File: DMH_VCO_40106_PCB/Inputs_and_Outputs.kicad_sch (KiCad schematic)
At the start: 13 parts, among them J1 TS_Jack_6.35mm_Sw, J150 Conn_01x12, J2 TS_Jack_6.35mm_Sw, J200 IDC_02x05, J3 TS_Jack_6.35mm_Sw, J4 TS_Jack_6.35mm_Sw, J5 TS_Jack_6.35mm_Sw, J6 TS_Jack_6.35mm_Sw, J7 TS_Jack_6.35mm_Sw, J8 TS_Jack_6.35mm_Sw, J9 TS_Jack_6.35mm_Sw, SW1 SW_SPDT_321_OnOff, SW2 SW_SPDT_321_OnOff

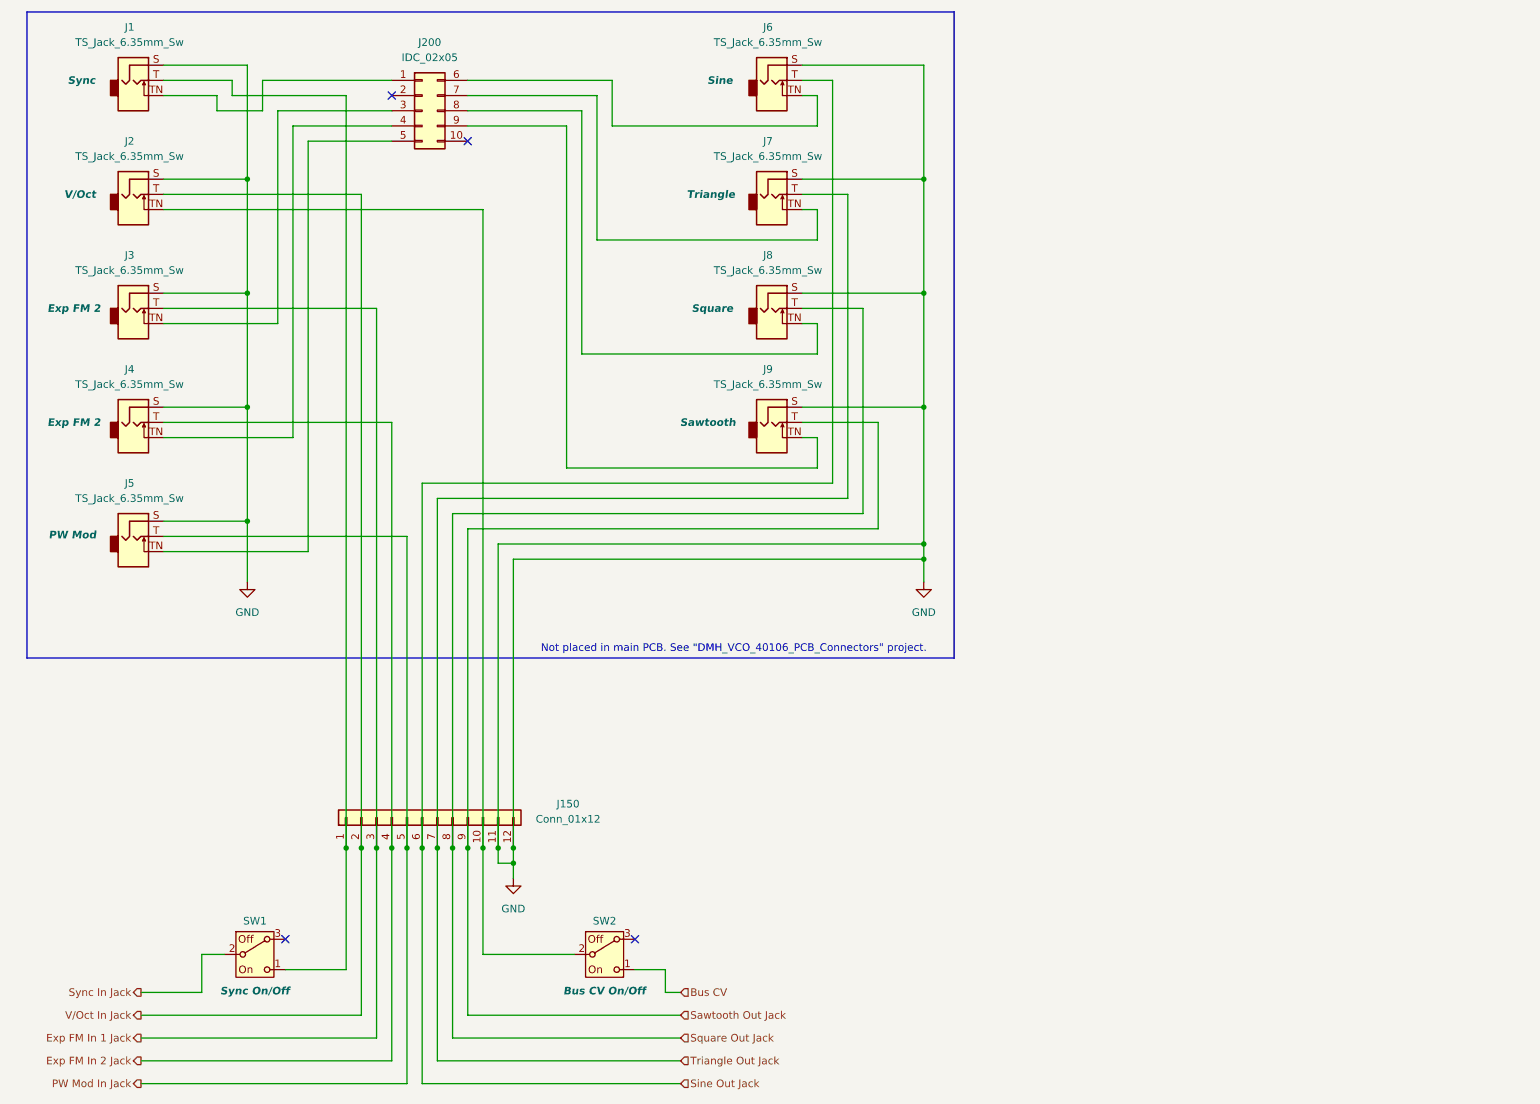
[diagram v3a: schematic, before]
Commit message: Added V/Oct input buffering to main schematic
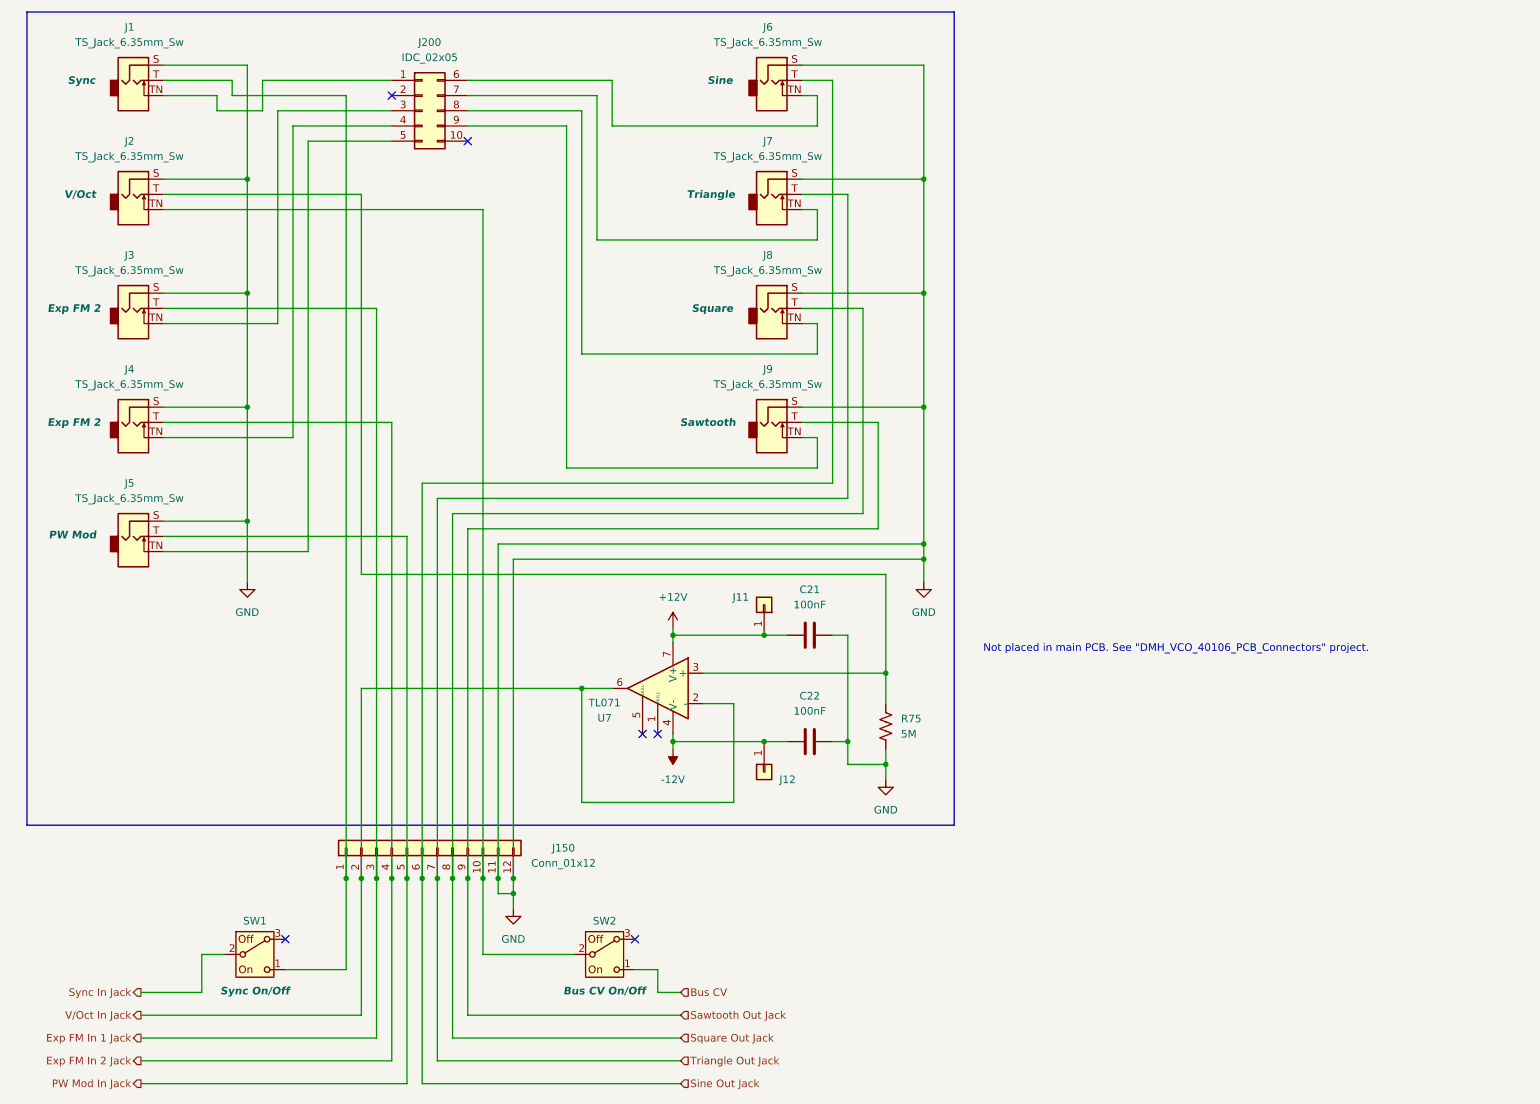
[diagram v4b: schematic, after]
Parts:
- added C21, C22: 100nF, Capacitor_THT:C_Disc_D4.3mm_W1.9mm_P5.00mm, symbol Device:C
- added J11, J12: Conn_01x01, Connector_PinHeader_2.54mm:PinHeader_1x01_P2.54mm_Vertical, symbol Connector_Generic:Conn_01x01
- added R75: 5M, Resistor_THT:R_Axial_DIN0207_L6.3mm_D2.5mm_P7.62mm_Horizontal, symbol Device:R_US
- added U7: TL071, Package_DIP:DIP-8_W7.62mm_Socket, symbol Amplifier_Operational:TL071
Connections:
- net GND: now also C21.2, C22.2, R75.1
- net V/Oct In Jack: now also U7.2 (-), U7.6; no longer J2.T
- new net: J2.T, R75.2, U7.3 (+)
- new net +12V: C21.1, J11.1 (Pin_1), U7.7 (V+)
- new net -12V: C22.1, J12.1 (Pin_1), U7.4 (V-)
- no-connect marks 4 -> 6
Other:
- moved on the sheet: J150

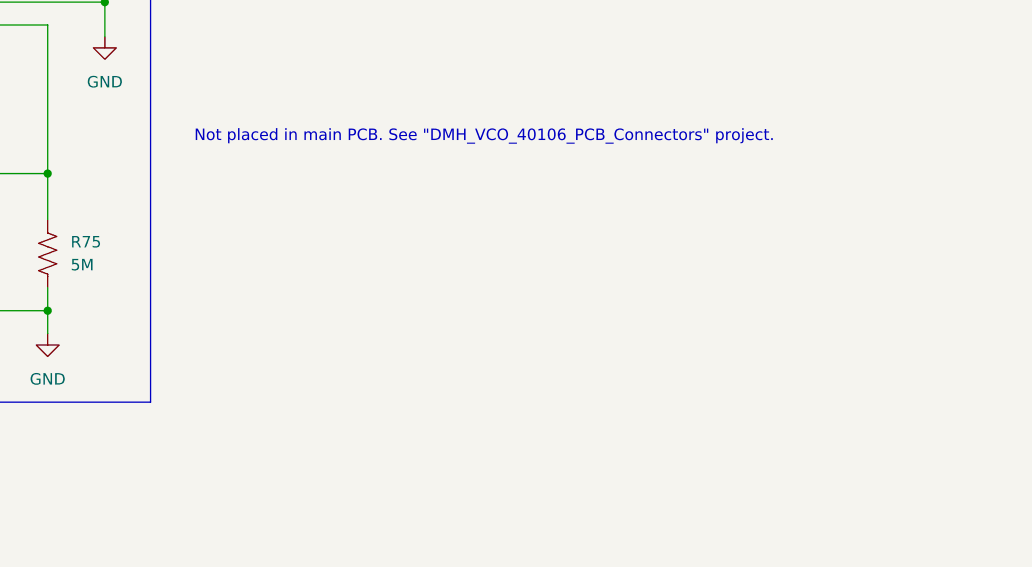
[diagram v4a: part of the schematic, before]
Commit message: Added info about jumpers to main PCB schematic
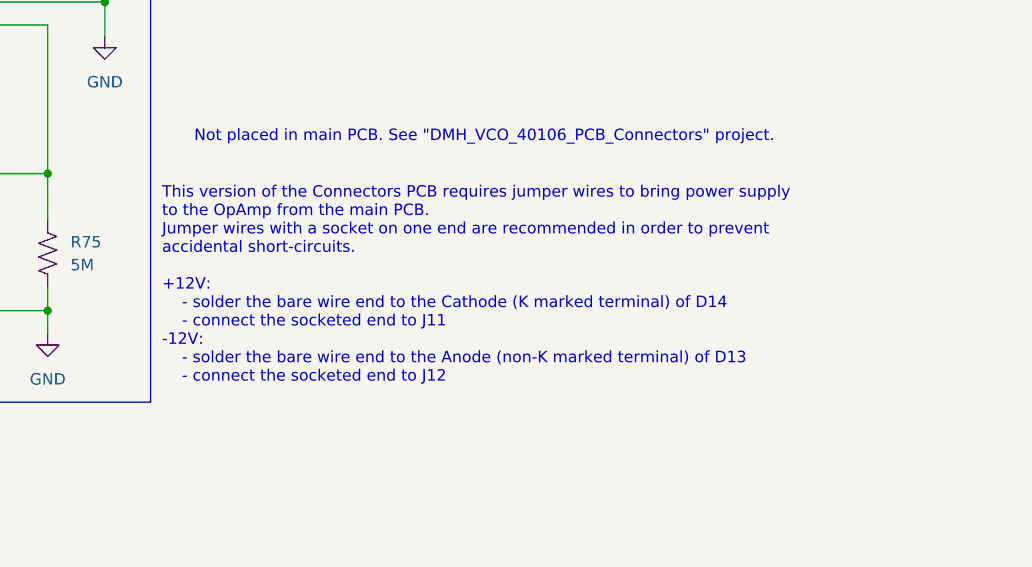
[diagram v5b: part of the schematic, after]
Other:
- note added: "This version of the Connectors PCB requires jumper wires to bring power supply to the OpAmp from the main PCB. Jumper wires with a socket on one end are recommended in order to prevent accidental short-circuits. +12V: - solder the bare wire end to the Cathode (K marked terminal) of D14 - connect the socketed end to J11 -12V: - solder the bare wire end to the Anode (non-K marked terminal) of D13 -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"
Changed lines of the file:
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@@
+		)
+	)
+	(text "This version of the Connectors PCB requires jumper wires to bring power supply\nto the OpAmp from the main PCB.\nJumper wires with a socket on one end are recommended in order to prevent\naccidental short-circuits.\n\n+12V:\n	- solder the bare wire end to the Cathode (K marked terminal) of D14\n	- connect the socketed end to J11\n-12V:\n	- solder the bare wire end to the Anode (non-K marked terminal) of D13\n	- connect the socketed end to J12"
+		(exclude_from_sim no)
+		(at 203.2 136.906 0)
+		(effects
+			(font
+				(size 1.27 1.27)
+			)
+			(justify left)
 		)
 	)
